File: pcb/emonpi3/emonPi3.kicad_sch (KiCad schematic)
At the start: 180 parts, among them CN1 CONN_03SCREW, CN2 CONN_03SCREW, CN3 CONN_03SCREW, J1 SJ-3524-SMT-TR, J10 Conn_02x13_Odd_Even, J11 Conn_ARM_JTAG_SWD_10, J12 CONN_04PTH, J13 Conn_01x03, J2 SJ-3524-SMT-TR, J3 SJ-3524-SMT-TR, J4 SJ-3524-SMT-TR, J5 SJ-3524-SMT-TR, J6 SJ-3524-SMT-TR, J7 CONN_04PTH, J8 USB_C_Receptacle_USB2.0, SW1 SW_Push, SW2 SW_Push, SW3 SW_Push, U1 AP2112K-3.3, U2 RFM69CW, U3 ATSAMD21J16A-M, U4 MCP1501-10xCH, U5 USBLC6-2P6, U6 24AA02-OT, U8 LMV331

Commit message: * Tidy schematic
* Rename to emonPi3

* Correct license on schematic (CC-SA 4.0 International)
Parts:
- C1, C10, C16, C2, C3, C4, C5, C6, C7, C8, C9: value 10uF 6V -> 10uF; Voltage (none) -> 6V
- C11, C14, C15, C39, C40: value 1uF 6V -> 1uF; Voltage (none) -> 16V
- R35, R36, R40, R42, R50, R56: Tolerance (none) -> 0.1%
- R53, R54: value 1K -> 10K
- R67: now not fitted
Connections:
- net V_REF is gone; now on net V_{REF}: ANALOG_EXPANDER0.3 (Pin_3), R36.2
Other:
- note added: "Hardware design files are licensed under the Creative Commons Attribution-ShareAlike 4.0 License Design is provided "AS IS" and "WITH ALL FAULTS. OpenEnergyMonitor DISCLAIMS ALL OTHER WARRANTIES, EXPRESS OR IMPLIED,"
- note removed: "1/4 and 3/4 VREF for ADC calibration"
- note removed: "Hardware design files are licensed under the Creative Commons Attribution-ShareAlike 3.0 Unported License Design is provided "AS IS" and "WITH ALL FAULTS. OpenEnergyMonitor DISCLAIMS ALL OTHER WARRANTIES, EXPRESS OR IMPLIED,"
- title: emon32-Pi2 -> emonPi3
- moved on the sheet: ANALOG_EXPANDER0, C1, C10, C12, C13, C16, C17, C19, C2, C20, C23, C24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

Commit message: * Final touch up for manufacture
  - BoM generation as part of script
  - Tidy up README
  - Correct part reference for ATSAMD21J17 in schematic
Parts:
- R67: now fitted
- U3: value ATSAMD21J16A-M -> ATSAMD21J17A-M; symbol MCU_Microchip_SAMD:ATSAMD21J16A-M -> MCU_Microchip_SAMD:ATSAMD21J17A-M
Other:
- note added: "Hardware design files are licensed under the Creative Commons Attribution-ShareAlike 4.0 License Design is provided "AS IS" and "WITH ALL FAULTS. ALL OTHER WARRANTIES, EXPRESS OR IMPLIED, ARE DISCLAIMED."
- note removed: "Hardware design files are licensed under the Creative Commons Attribution-ShareAlike 4.0 License Design is provided "AS IS" and "WITH ALL FAULTS. OpenEnergyMonitor DISCLAIMS ALL OTHER WARRANTIES, EXPRESS OR IMPLIED,"
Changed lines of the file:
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@@
   (title_block
     (title "emonPi3")
-    (date "2024-02-16")
+    (date "2024-02-25")
     (rev "v0.1")
     (company "OpenEnergyMonitor / Tilt Ltd (Angus Logan)")
@@
     (effects (font (size 1.27 1.27)) (justify left top))
   )
-  (text_box "Hysteresis:\n575 mV L->H\n506 mV H->L"
-    (at 539.75 260.35 0) (size 16.51 7.62)
+  (text_box "Hysteresis:\n575 mV L->H\n506 mV H->L\n\nRemoves positive edge on negative transition."
+    (at 539.75 260.35 0) (size 24.13 13.97)
     (stroke (width 0) (type default))
     (fill (type none))
@@
     (effects (font (size 2 2) (thickness 0.4) bold) (justify left bottom))
   )
-  (text "Hardware design files are licensed under the Creative Commons Attribution-ShareAlike 4.0 License\nDesign is provided \"AS IS\" and \"WITH ALL FAULTS. OpenEnergyMonitor DISCLAIMS ALL OTHER WARRANTIES, EXPRESS OR IMPLIED,"
+  (text "Hardware design files are licensed under the Creative Commons Attribution-ShareAlike 4.0 License\nDesign is provided \"AS IS\" and \"WITH ALL FAULTS. ALL OTHER WARRANTIES, EXPRESS OR IMPLIED, ARE DISCLAIMED."
     (at 31.75 398.78 0)
     (effects (font (size 1.65 1.65)) (justify left bottom))
@@
   )
   (symbol (lib_id "Device:R") (at 530.86 271.78 90) (mirror x) (unit 1)
-    (in_bom yes) (on_board yes) (dnp yes)
+    (in_bom yes) (on_board yes) (dnp no)
     (property "Reference" "R67" (at 528.32 270.51 90)
       (effects (font (size 1.27 1.27)) (justify right bottom))
@@
     )
   )
-  (symbol (lib_id "MCU_Microchip_SAMD:ATSAMD21J16A-M") (at 257.81 213.36 0) (unit 1)
+  (symbol (lib_id "MCU_Microchip_SAMD:ATSAMD21J17A-M") (at 257.81 213.36 0) (unit 1)
     (in_bom yes) (on_board yes) (dnp no) (fields_autoplaced)
     (property "Reference" "U3" (at 262.3059 261.62 0)
       (effects (font (size 1.27 1.27)) (justify left))
     )
-    (property "Value" "ATSAMD21J16A-M" (at 262.3059 264.16 0)
+    (property "Value" "ATSAMD21J17A-M" (at 262.3059 264.16 0)
       (effects (font (size 1.27 1.27)) (justify left))
     )

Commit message: * Replace RPi header with SMD
* Replace Cortex-M 10pin with SMD
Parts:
- removed J13: Conn_01x03, Connector_PinHeader_2.54mm:PinHeader_1x03_P2.54mm_Vertical, symbol Connector_Generic:Conn_01x03
- added C39: 100nF, Capacitor_SMD:C_0603_1608Metric, symbol Device:C
- J10: renamed from J11; footprint Connector_PinHeader_1.27mm:PinHeader_2x05_P1.27mm_Vertical -> Connector_PinHeader_1.27mm:PinHeader_2x05_P1.27mm_Vertical_SMD; now not fitted
- J11: renamed from J10; footprint Connector_PinSocket_2.54mm:PinSocket_2x13_P2.54mm_Vertical -> RPi-SMD:REF-182688
- renumbered C27 to C1, C35 to C10, C17 to C11, C24 to C12, C25 to C13, C26 to C14, C29 to C15, C30 to C16, C36 to C17, C37 to C18, C7 to C19, C28 to C2, C8 to C20, C9 to C21, C31 to C22, C32 to C23, C33 to C24, C11 to C25, C39 to C26, C19 to C27, C14 to C28, C16 to C29, C1 to C3, C15 to C30, C21 to C31, C34 to C32, C18 to C33, C12 to C34, C40 to C35, C13 to C36, C20 to C37, C10 to C38, C2 to C4, C23 to C40, C38 to C41, C3 to C5, C4 to C6, C5 to C7, C6 to C8, C22 to C9, GND_LINK0 to GND_LINK1, ANALOG_EXPANDER0 to J12, J12 to J7, J7 to J8, J8 to J9, LED0 to LED1, LED1 to LED2, LED2 to LED3, LED3 to LED4, R7 to R10, R16 to R11, R8 to R12, R17 to R13, R9 to R14, R18 to R15, R10 to R16, R19 to R17, R11 to R18, R20 to R19, R12 to R20, R25 to R22, R26 to R23, R27 to R24, R28 to R25, R29 to R26, R30 to R27, R36 to R28, R56 to R29, R42 to R30, R50 to R31, R43 to R32, R13 to R33, R22 to R34, R14 to R35, R23 to R36, R15 to R37, R24 to R38, R31 to R39, R32 to R40, R33 to R41, R35 to R42, R40 to R43, R52 to R44, R39 to R45, R34 to R46, R68 to R47, R69 to R48, R51 to R49, R59 to R50, R57 to R51, R60 to R52, R58 to R53, R47 to R54, R54 to R56, R53 to R57, R61 to R58, R44 to R59, R45 to R60, R46 to R61, R63 to R62, R41 to R63, R65 to R64, R66 to R65, R49 to R66, R48 to R67, R67 to R68, R64 to R69, R62 to R7, R37 to R8, R38 to R9, RJ45 to RJ1, SMA0 to SMA1, SW3 to SW2, SW2 to SW3, TP12 to TP10, TP13 to TP11, TP7 to TP12, TP8 to TP13, TP5 to TP3, TP3 to TP4, TP4 to TP5, TP9 to TP6, TP10 to TP7, TP11 to TP8, TP6 to TP9, U4 to U1, U5 to U2, U1 to U4, U7 to U5, U8 to U6, U2 to U7, U6 to U8
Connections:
- net +5V: now also C39.1
- net GND: now also C39.2
- net RFM_MISO: now also R60.1; no longer R60.2
- net RFM_MISO_UC: now also R60.2; no longer R60.1
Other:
- note removed: "UART"
- moved on the sheet: R60

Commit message: * Software select of OneWire or pulse input
  - https://community.openenergymonitor.org/t/whats-happened-to-emontx-v4/25775/22
  - Add pull up resistors on GPIO pins, rather than hard wiring
  - Move revision pin REV_0 to pin 1
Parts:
- removed SL1, SL3: JUMPER-SMT_2_NC_PASTE_NO-SILK, Jumper:SolderJumper-2_P1.3mm_Open_TrianglePad1.0x1.5mm, symbol Jumper:SolderJumper_2_Open
- removed SL2, SL4: SOLDERJUMPERNC, Jumper:SolderJumper-2_P1.3mm_Open_TrianglePad1.0x1.5mm, symbol Jumper:SolderJumper_2_Open
- added R70: 3K3, Resistor_SMD:R_0603_1608Metric, symbol Device:R
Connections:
- net PULSE1 is gone; now on net P_OW_1: J11.13 (Pin_13), U3.36 (PA17)
- net PULSE2 is gone; now on net P_OW_2: J11.15 (Pin_15), U3.35 (PA16)
- net +3V3: no longer R32.1
- net GND: now also U3.1 (PA00); no longer U3.38 (PA19)
- net P_OW_2: now reaches CN1.2 (Pin_2)
- net P_OW_2: now also R70.2
- net P_OW_1: now reaches CN2.2 (Pin_2)
- net P_OW_1: now also R32.2
- removed net DS18B20: J11.11 (Pin_11), R32.2, U3.37 (PA18)
- new net P_OW_1_PU: R32.1, U3.37 (PA18)
- new net P_OW_2_PU: R70.1, U3.38 (PA19)

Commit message: * Connect RFM module reset and IRQ
  - https://community.openenergymonitor.org/t/whats-happened-to-emontx-v4/25775/28
  - Connect microcontroller to reset and IRQ from RFM
  - Reroute USB sense
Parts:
- R70: value 3K3 -> 22R
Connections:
- net P_OW_1: now also U3.35 (PA16); no longer U3.36 (PA17)
- net RFM_IRQ: now also U3.27 (PB14)
- net RFM_RESET: now also R70.2
- net VUSB_SENSE: now also U3.38 (PA19); no longer U3.27 (PB14)
- net P_OW_2 renamed PULSE2
- net PULSE2: now also U3.36 (PA17); no longer R70.2, U3.35 (PA16)
- net P_OW_2_PU renamed RFM_RESET_UC
- net RFM_RESET_UC: now also U3.28 (PB15); no longer U3.38 (PA19)
- net ~{RPI_PRESENT}: no longer names the net of J11.25 (Pin_25)
- net ~{RPI_PRESENT}: no longer U3.28 (PB15)
- no-connect marks 22 -> 23

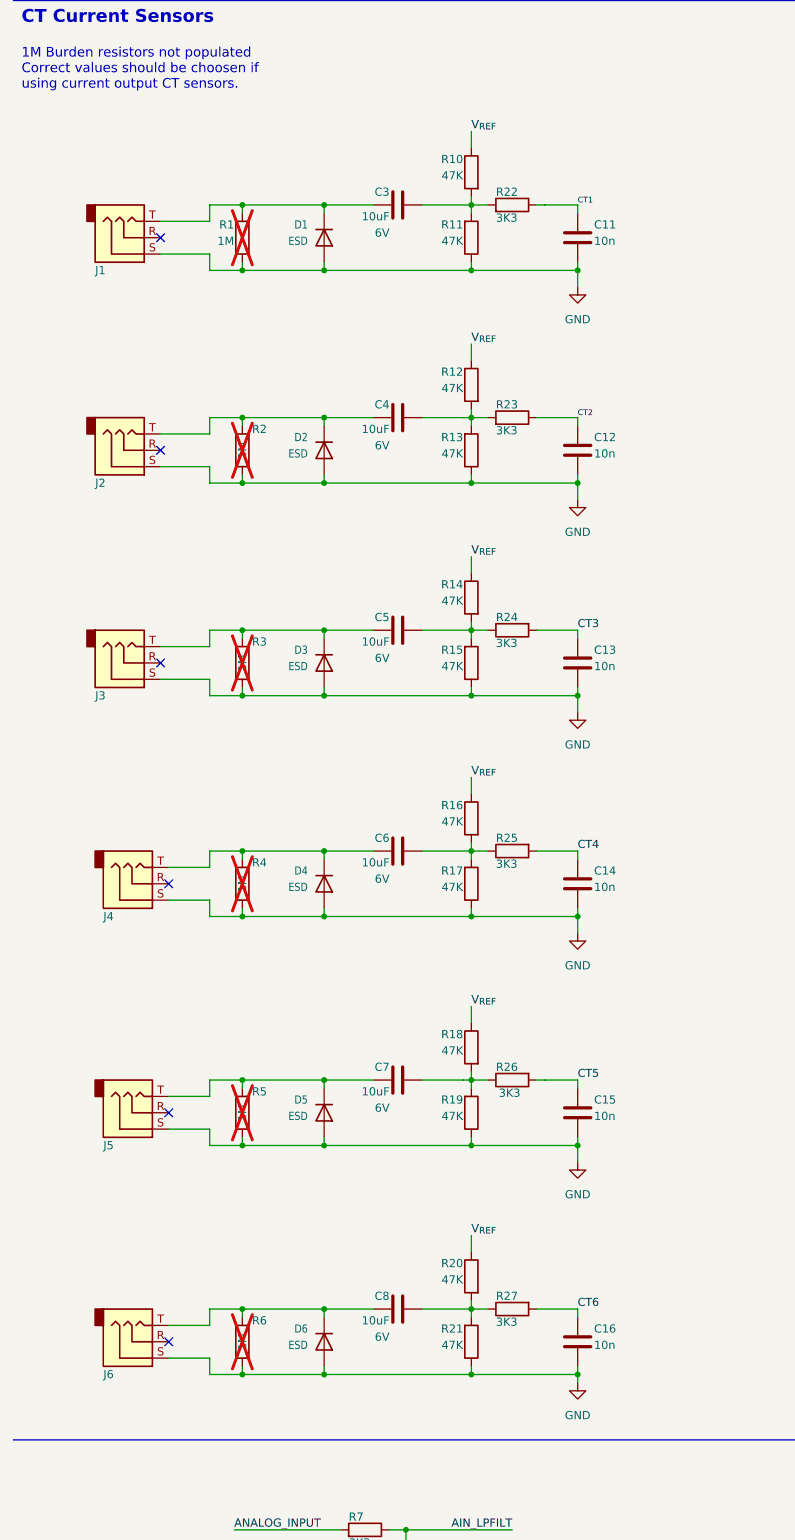
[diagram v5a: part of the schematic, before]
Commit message: * Add jumpers to connect CT burden resistors
  - https://community.openenergymonitor.org/t/whats-happened-to-emontx-v4/25775/28
  - Allows use of current output CTs which may already be in use
  - "Refactor" the common CT frontend into a separate hierarchy
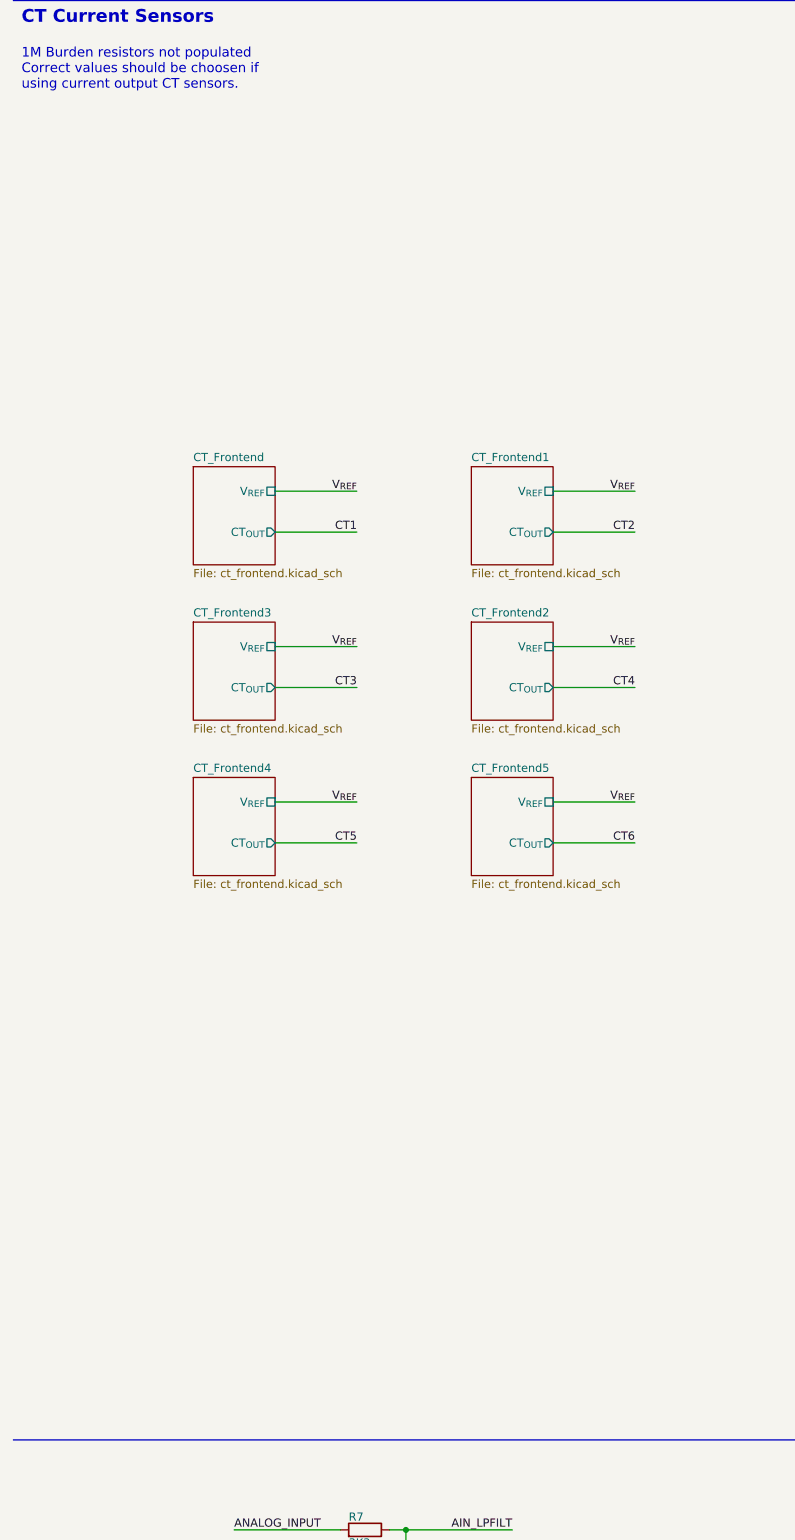
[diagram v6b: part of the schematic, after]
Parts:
- removed C11, C12, C13, C14, C15, C16: 10n, Capacitor_SMD:C_0603_1608Metric, symbol Device:C
- removed C3, C4, C5, C6, C7, C8: 10uF, Capacitor_SMD:C_0603_1608Metric, symbol Device:C
- removed D1, D2, D3, D4, D5, D6: ESD, Diode_SMD:D_SOD-523, symbol Device:D
- removed J1, J2, J3, J4, J5, J6: SJ-3524-SMT-TR, Connector_Audio:Jack_3.5mm_CUI_SJ-3524-SMT_Horizontal, symbol Connector_Audio:AudioJack3
- removed R1, R2, R3, R4, R5, R6: 1M, Resistor_SMD:R_1206_3216Metric, symbol Device:R
- removed R10, R11, R12, R13, R14, R15, R16, R17, R18, R19, R20, R21: 47K, Resistor_SMD:R_0603_1608Metric, symbol Device:R
- removed R22, R23, R24, R25, R26, R27: 3K3, Resistor_SMD:R_0603_1608Metric, symbol Device:R
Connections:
- no-connect marks 23 -> 17
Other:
- added sheet CT_Frontend (ct_frontend.kicad_sch)
- added sheet CT_Frontend1 (ct_frontend.kicad_sch)
- added sheet CT_Frontend2 (ct_frontend.kicad_sch)
- added sheet CT_Frontend3 (ct_frontend.kicad_sch)
- added sheet CT_Frontend4 (ct_frontend.kicad_sch)
- added sheet CT_Frontend5 (ct_frontend.kicad_sch)

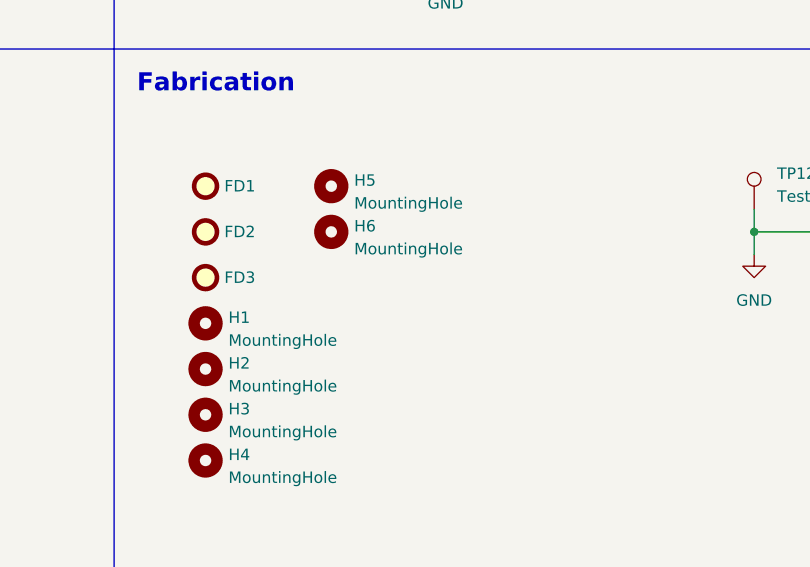
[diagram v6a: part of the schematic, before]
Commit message: * Add mounting hole for OLED
  - For https://www.aliexpress.com/item/32957309383.html
  - https://community.openenergymonitor.org/t/whats-happened-to-emontx-v4/25775/22
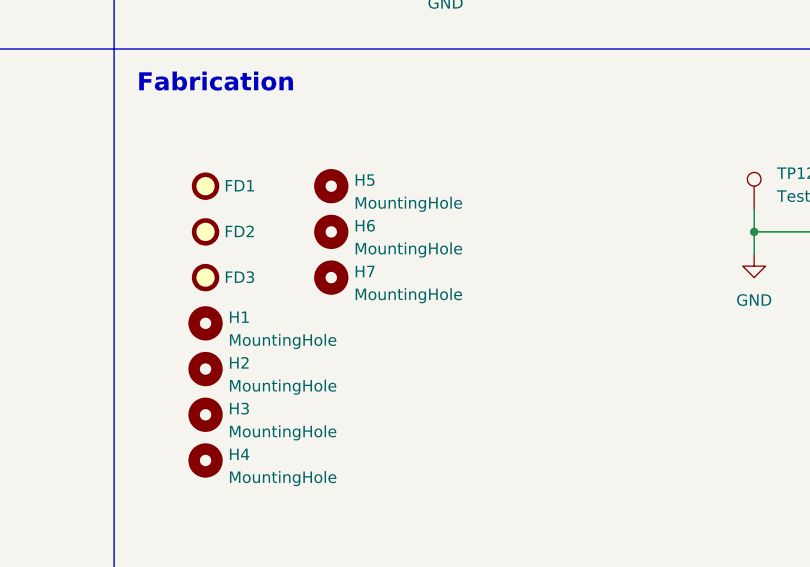
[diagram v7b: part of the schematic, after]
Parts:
- added H7: MountingHole, MountingHole:MountingHole_2.1mm, symbol Mechanical:MountingHole
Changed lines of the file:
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@@
+    )
+  )
+  (symbol (lib_id "Mechanical:MountingHole") (at 497.84 320.04 0) (unit 1)
+    (in_bom no) (on_board yes) (dnp no) (fields_autoplaced)
+    (property "Reference" "H7" (at 500.38 319.405 0)
+      (effects (font (size 1.27 1.27)) (justify left))
+    )
+    (property "Value" "MountingHole" (at 500.38 321.945 0)
+      (effects (font (size 1.27 1.27)) (justify left))
+    )
+    (property "Footprint" "MountingHole:MountingHole_2.1mm" (at 497.84 320.04 0)
+      (effects (font (size 1.27 1.27)) hide)
+    )
+    (property "Datasheet" "~" (at 497.84 320.04 0)
+      (effects (font (size 1.27 1.27)) hide)
+    )
+    (instances
+      (project "emonPi3"
+        (path "/3a5f1087-1abe-4575-9313-bd86a5e03366"
+          (reference "H7") (unit 1)
+        )
+      )
     )
   )
